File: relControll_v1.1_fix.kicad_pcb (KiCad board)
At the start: 2 copper layers, 196.2 x 67.3 mm, 40 parts, among them J1 left side, J2 right side, J3 Conn_01x06_Socket, J4 Conn_01x06_Socket, SW1 PEC11R-4015F-S0024, U1 74HC4051, U2 74HC4051, U3 6N137S_C20612601

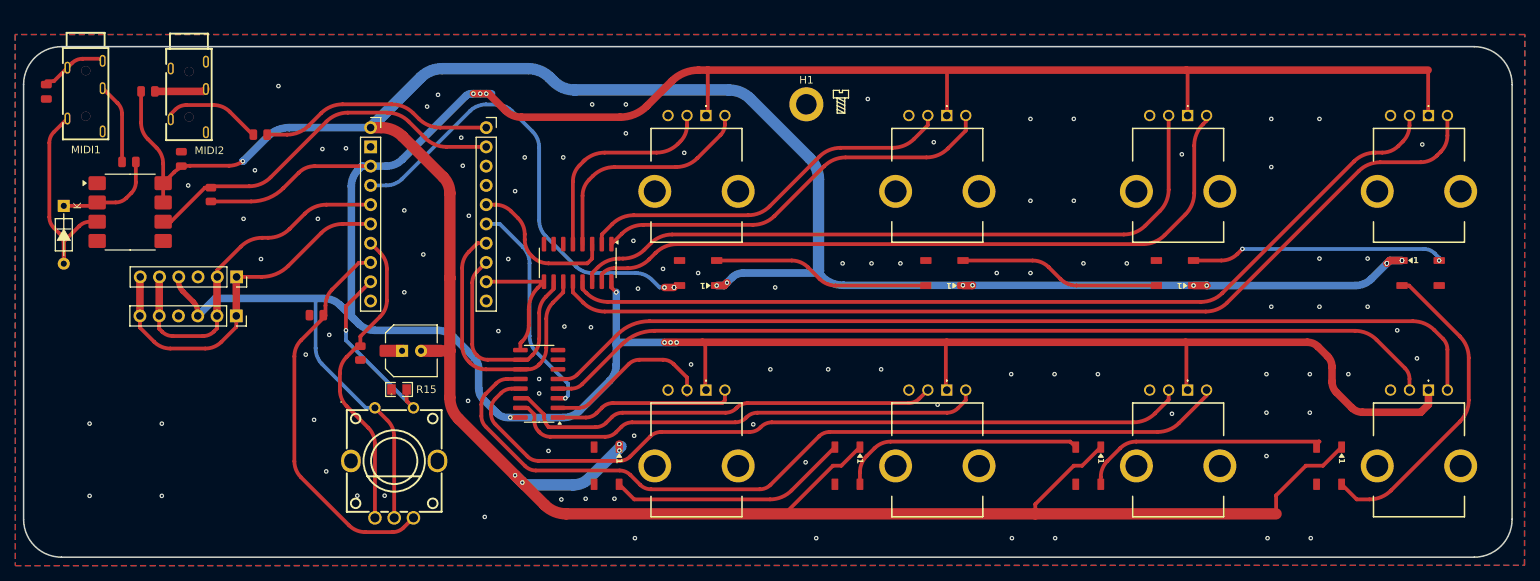
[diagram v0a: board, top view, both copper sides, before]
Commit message: new pcb design
changed footprint for esp32s3 zero devboard changed dual multiplexer to single 16ch multiplexer, changed some pins functions
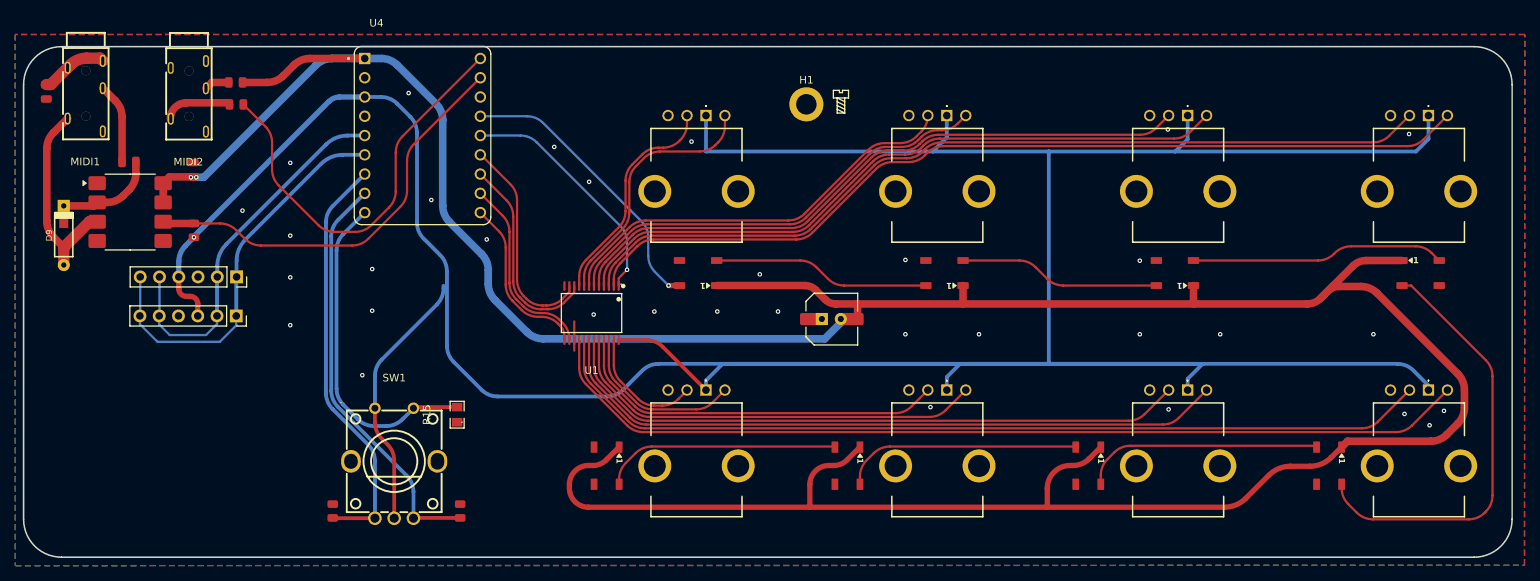
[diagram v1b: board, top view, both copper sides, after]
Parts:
- removed J1: left side, Connector_PinSocket_2.54mm:PinSocket_1x10_P2.54mm_Vertical
- removed J2: right side, Connector_PinSocket_2.54mm:PinSocket_1x10_P2.54mm_Vertical
- removed U2: 74HC4051, Package_SO:SOIC-16_3.9x9.9mm_P1.27mm
- added U4: ESP32-S3-ZERO, LibVrac:MODULE_ESP32-S3-ZERO, F.Cu at (102.1, 66.3)
- D9: footprint PCM_Diode_THT_AKL:D_DO-35_SOD27_P7.62mm_Horizontal -> keyboard_parts.pretty-master:D_SOD123_axial
- U1: value 74HC4051 -> CD74HC4067SM96; footprint Package_SO:SOIC-16_3.9x9.9mm_P1.27mm -> EasyEDA:SSOP-24_L8.1-W5.3-P0.65-LS7.8-BL
- moved C1 55.6 mm to (156.1, 90.5)
- moved C1 55.5 mm to (154.7, 90.5)
- moved R17 32.0 mm to (107.1, 115.8), turned to -90 degrees
- moved R16 21.1 mm to (90.3, 115.8), turned to -90 degrees
- moved R11 11.6 mm to (77.5, 59.3), turned to 180 degrees
- moved R15 8.35 mm to (106.7, 103.1), turned to 90 degrees
- moved U1 6.86 mm to (124.4, 89.7), turned to 180 degrees
- moved R10 5.22 mm to (72.0, 78.8)
- moved R12 5.07 mm to (77.6, 62.2)
- moved D9 3.90 mm to (54.8, 79.5)
- moved C3 2.11 mm to (71.9, 70.8)
- moved MIDI2 0.08 mm to (71.2, 61.2)
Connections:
- net /ring2 renamed /MIDI IO/ring2
- net /sleeve renamed /MIDI IO/sleeve
- net /tip2 renamed /MIDI IO/tip2
- H1 pad 1: (no net) -> GND
- U1 pad 1: B5 -> ADC1
- U1 pad 10: S2 -> ADC2/S0
- U1 pad 12: B4 -> GND
- U1 pad 13: B1 -> S3
- U1 pad 14: B2 -> S2
- U1 pad 15: B3 -> GND
- U1 pad 16: VCC -> A8
- U1 pad 2: B7 -> B8
- U1 pad 3: ADC1 -> B7
- U1 pad 4: B8 -> B6
- U1 pad 5: B6 -> B5
- U1 pad 6: GND -> B4
- U1 pad 7: GND -> B3
- U1 pad 8: GND -> B2
- U1 pad 9: S3 -> B1
- VR1 pad 2: B6 -> B1
- VR1 pad A2: B8 -> B2
- VR2 pad 2: B7 -> B3
- VR2 pad A2: B5 -> B4
- VR3 pad 2: B2 -> B5
- VR3 pad A2: B3 -> B6
- VR4 pad 2: B1 -> B7
- VR4 pad A2: B4 -> B8
- VR5 pad 2: A7 -> A1
- VR5 pad A2: A5 -> A2
- VR6 pad 2: A2 -> A3
- VR6 pad A2: A3 -> A4
- VR7 pad 2: A1 -> A5
- VR7 pad A2: A4 -> A6
- VR8 pad 2: A8 -> A7
- VR8 pad A2: A6 -> A8
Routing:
- net A7: track 22.6 -> 118.1 mm
- net B1: track 121.5 -> 29.3 mm
- net B8: track 30.8 -> 119.5 mm
- net A1: track 102.1 -> 16.3 mm
- net B4: track 129.9 -> 58.7 mm
- net B7: track 50.7 -> 115.1 mm
- net B6: track 28.8 -> 89.1 mm
- net A5: track 24.1 -> 84.2 mm
- net B2: track 91.5 -> 33.8 mm
- net A4: track 113.5 -> 56.3 mm
- net B3: track 94.3 -> 55.3 mm
- net A6: track 127.1 -> 90.3 mm
- net A2: track 57.4 -> 22.4 mm
- net B5: track 54.1 -> 84.8 mm
- net ADC2: track 29.3 -> 0.00 mm, vias 1 -> 0
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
